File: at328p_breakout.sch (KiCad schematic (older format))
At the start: 1 part

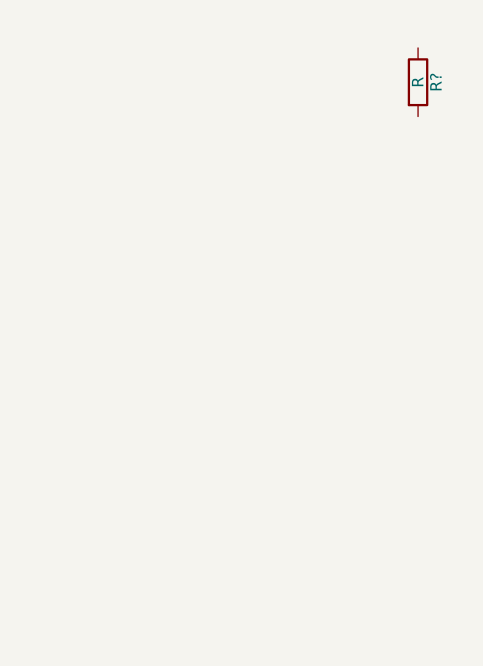
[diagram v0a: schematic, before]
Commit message: modified:   at328p_breakout-cache.lib 	modified:   at328p_breakout.pro 	modified:   at328p_breakout.sch
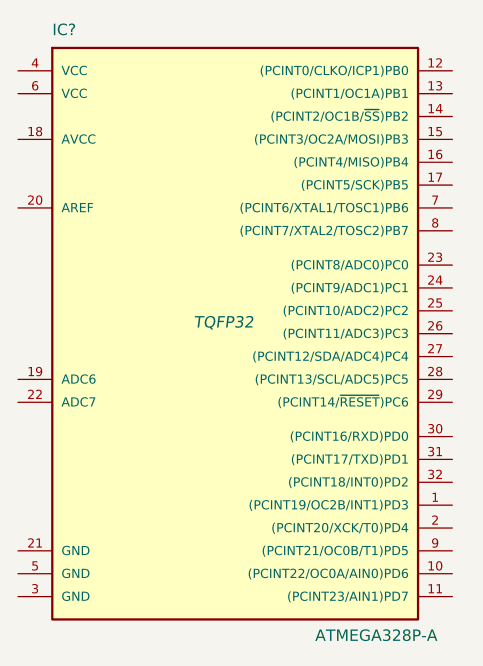
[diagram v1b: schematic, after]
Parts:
- removed R?: R, symbol R
- added IC?: ATMEGA328P-A, TQFP32, symbol ATMEGA328P-A
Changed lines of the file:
@@
 LIBS:contrib
 LIBS:valves
+LIBS:at328p_breakout-cache
 EELAYER 25 0
 EELAYER END
@@
 $EndDescr
 $Comp
-L R R?
-U 1 1 577693DF
-P 6750 2750
-F 0 "R?" V 6830 2750 50  0000 C CNN
-F 1 "R" V 6750 2750 50  0000 C CNN
-F 2 "" V 6680 2750 50  0000 C CNN
-F 3 "" H 6750 2750 50  0000 C CNN
-	1    6750 2750
+L ATMEGA328P-A IC?
+U 1 1 5776B530
+P 5900 3800
+F 0 "IC?" H 5150 5050 50  0000 L BNN
+F 1 "ATMEGA328P-A" H 6300 2400 50  0000 L BNN
+F 2 "TQFP32" H 5900 3800 50  0000 C CIN
+F 3 "" H 5900 3800 50  0000 C CNN
+	1    5900 3800
 	1    0    0    -1
 $EndComp
